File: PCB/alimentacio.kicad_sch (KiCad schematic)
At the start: 10 parts, among them J1 PowerIN, U1 LT1528CT-PBF

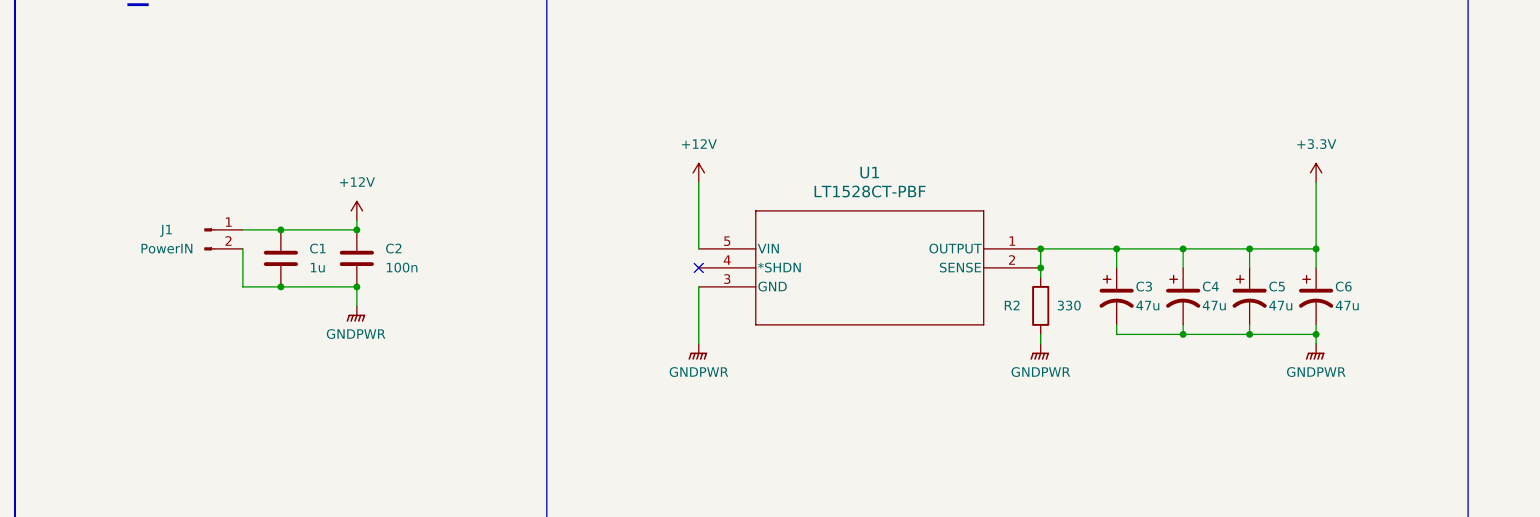
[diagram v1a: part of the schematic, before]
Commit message: correct schematic + README
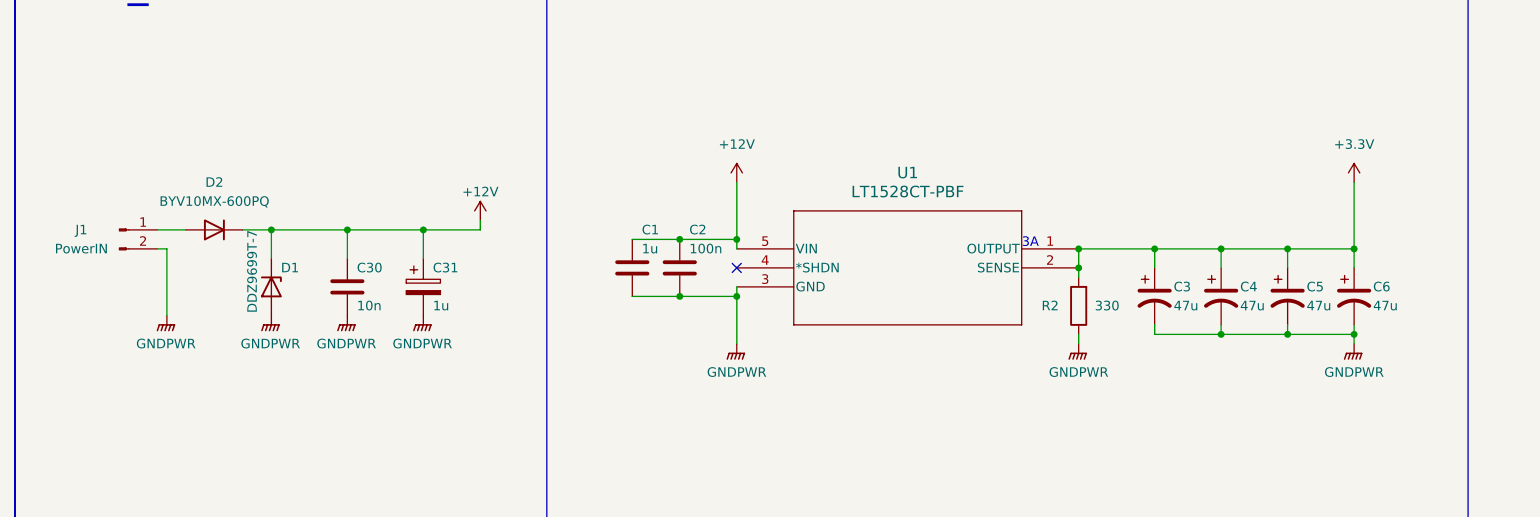
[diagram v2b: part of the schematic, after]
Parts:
- added C30: 10n, symbol Device:C
- added C31: 1u, symbol Device:C_Polarized
- added D1: DDZ9699T-7, symbol Device:D_Zener
- added D2: BYV10MX-600PQ, symbol Device:D
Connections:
- net +12V: now also C30.1, C31.1, D1.1 (K), D2.1 (K); no longer J1.1 (Pin_1)
- net GNDPWR: now also C30.2, C31.2, D1.2 (A)
- new net: D2.2 (A), J1.1 (Pin_1)
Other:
- note added: "3A"
- moved on the sheet: C3, C4, C5, C6, J1, R2, U1

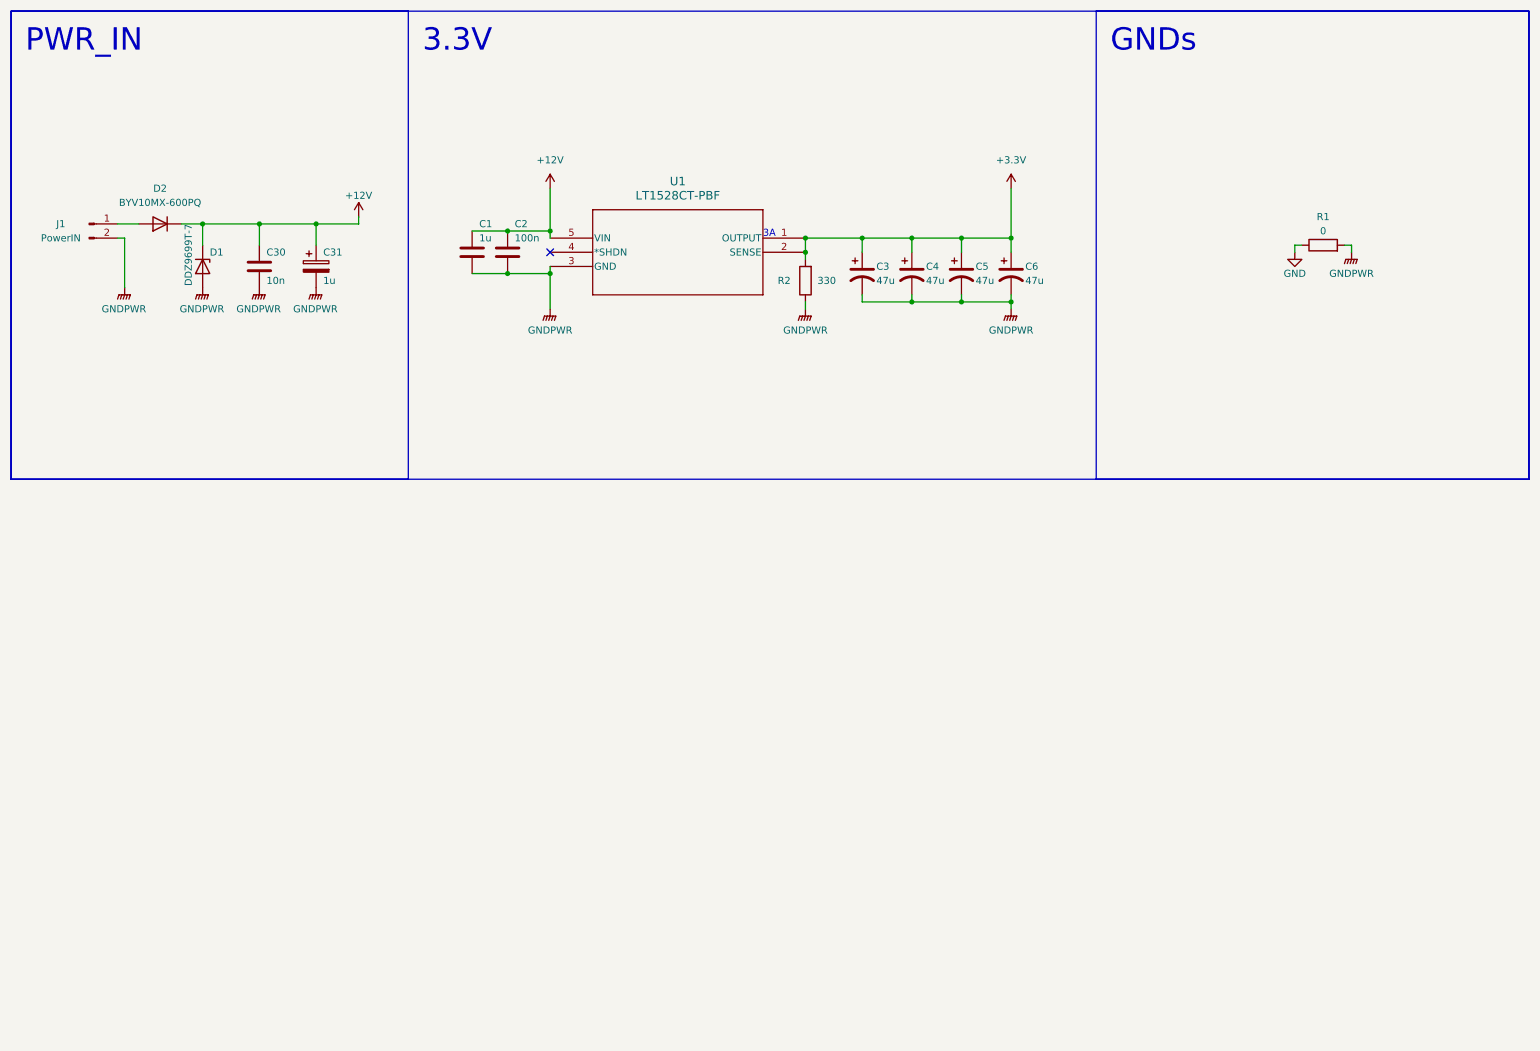
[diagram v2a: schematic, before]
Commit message: changed to DCDC 3.3V, added extra bit for window ctrl + misc corrections
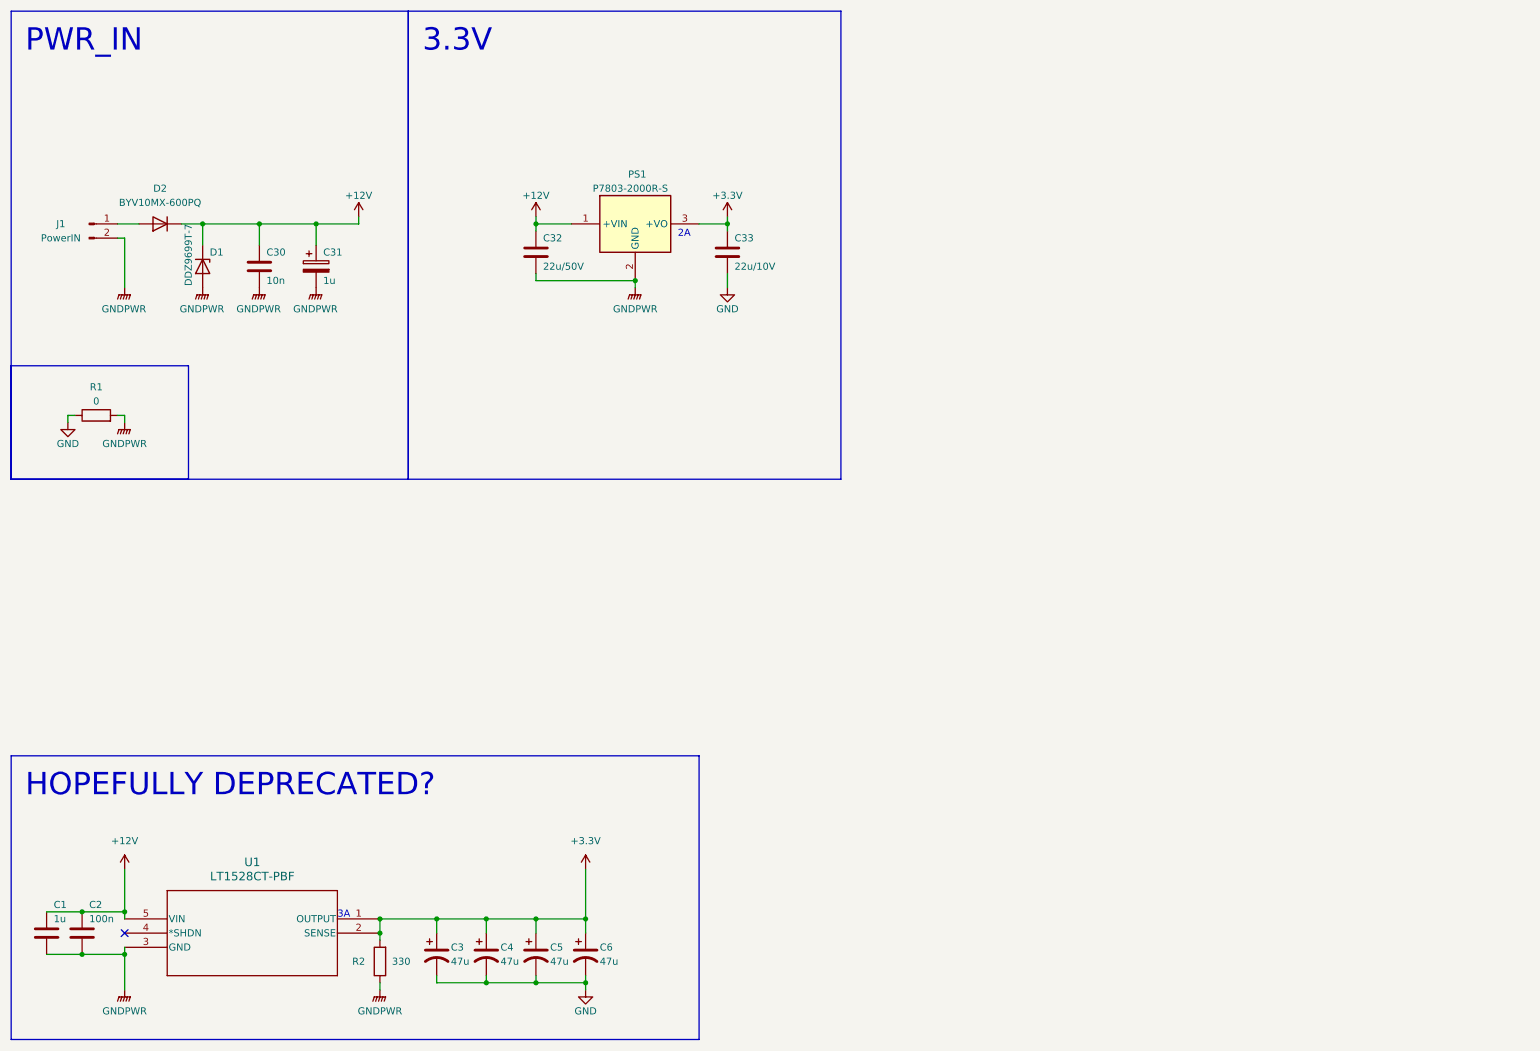
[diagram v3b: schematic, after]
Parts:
- added C32: 22u/50V, symbol Device:C
- added C33: 22u/10V, symbol Device:C
- added PS1: P7803-2000R-S, P78032000RS, symbol P7803-2000R-S:P7803-2000R-S
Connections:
- net +12V: now also C32.1, PS1.1 (+VIN)
- net +3.3V: now also C33.1, PS1.3 (+VO)
- net GND: now also C3.2, C4.2, C5.2, C6.2, C33.2
- net GNDPWR: now also C32.2, PS1.2 (GND); no longer C3.2, C4.2, C5.2, C6.2
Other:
- note added: "2A"
- note added: "HOPEFULLY DEPRECATED?"
- note removed: "GNDs"
- moved on the sheet: C1, C2, C3, C4, C5, C6, R1, R2, U1

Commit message: added all components
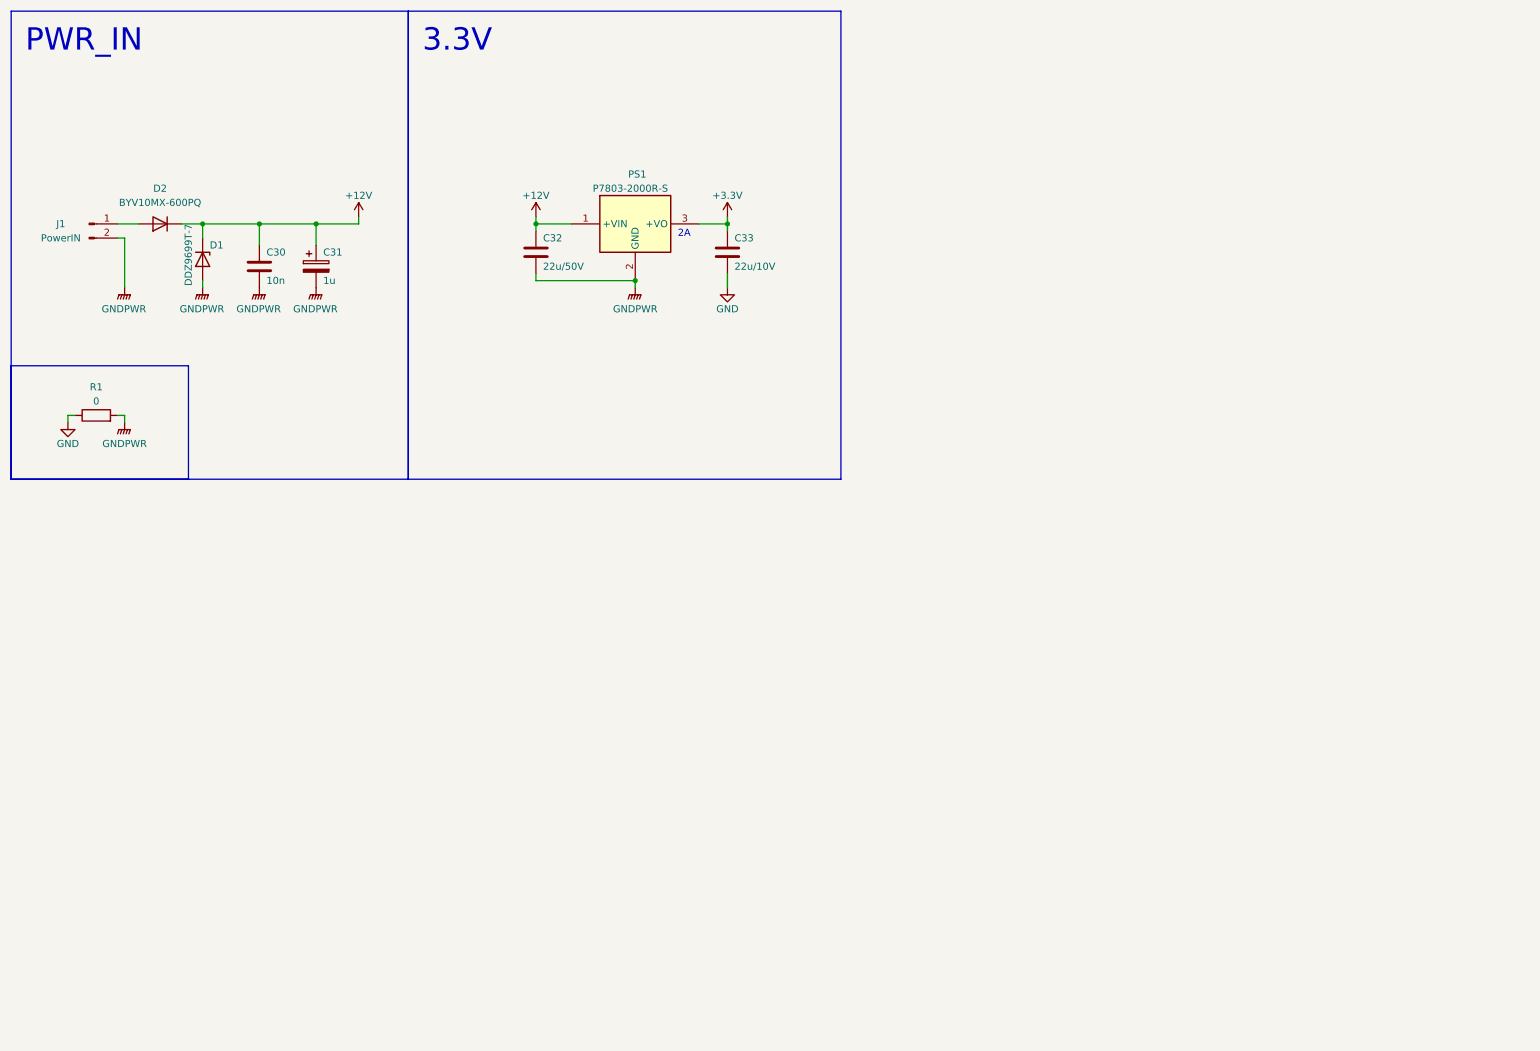
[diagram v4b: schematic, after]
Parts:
- removed C1: 1u, symbol Device:C
- removed C2: 100n, symbol Device:C
- removed C3, C4, C5, C6: 47u, symbol Device:C_Polarized_US
- removed R2: 330, symbol Device:R
- removed U1: LT1528CT-PBF, TO220-5_T_LIT, symbol LT1528CT#PBF:LT1528CT-PBF
- C30, C33: footprint (none) -> Capacitor_SMD:C_1206_3216Metric
- C31: footprint (none) -> Capacitor_Tantalum_SMD:CP_EIA-3216-18_Kemet-A
- C32: footprint (none) -> kicad_models:CAPC7563X400N
- D1: footprint (none) -> kicad_models:SODFL1608X65N
- D2: footprint (none) -> Package_TO_SOT_THT:TO-220F-2_Horizontal_TabDown
- J1: footprint (none) -> TerminalBlock_MetzConnect:TerminalBlock_MetzConnect_Type011_RT05502HBWC_1x02_P5.00mm_Horizontal
- PS1: footprint P78032000RS -> kicad_models:P78032000RS
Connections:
- no-connect marks 1 -> 0
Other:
- note removed: "3A"
- note removed: "HOPEFULLY DEPRECATED?"
- moved on the sheet: D1

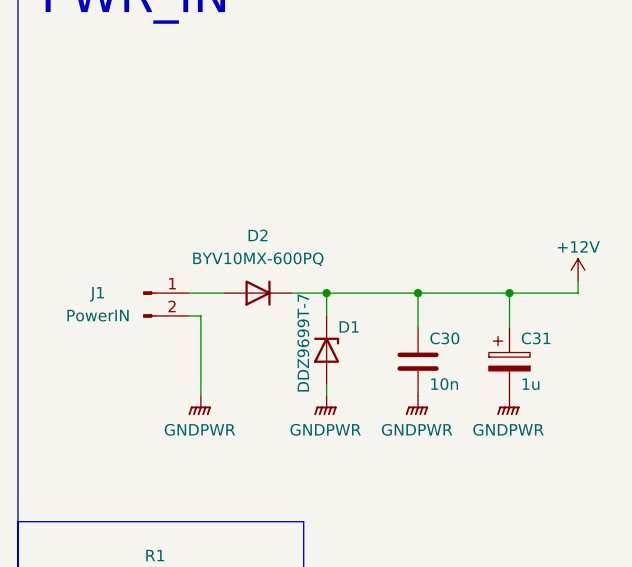
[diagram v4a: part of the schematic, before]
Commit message: power plane done
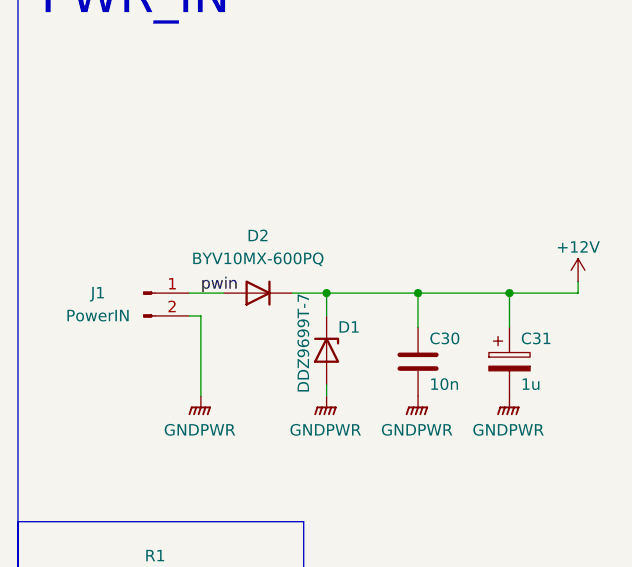
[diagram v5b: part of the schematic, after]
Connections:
- net pwin: now reaches D2.2 (A), J1.1 (Pin_1)
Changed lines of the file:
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@@
     (effects (font (size 4 4)) (justify left bottom))
+  )
+  (label "pwin" (at 33.02 50.8 0) (fields_autoplaced)
+    (effects (font (size 1.27 1.27)) (justify left bottom))
   )
   (symbol (lib_id "power:GNDPWR") (at 33.02 62.23 0) (unit 1)

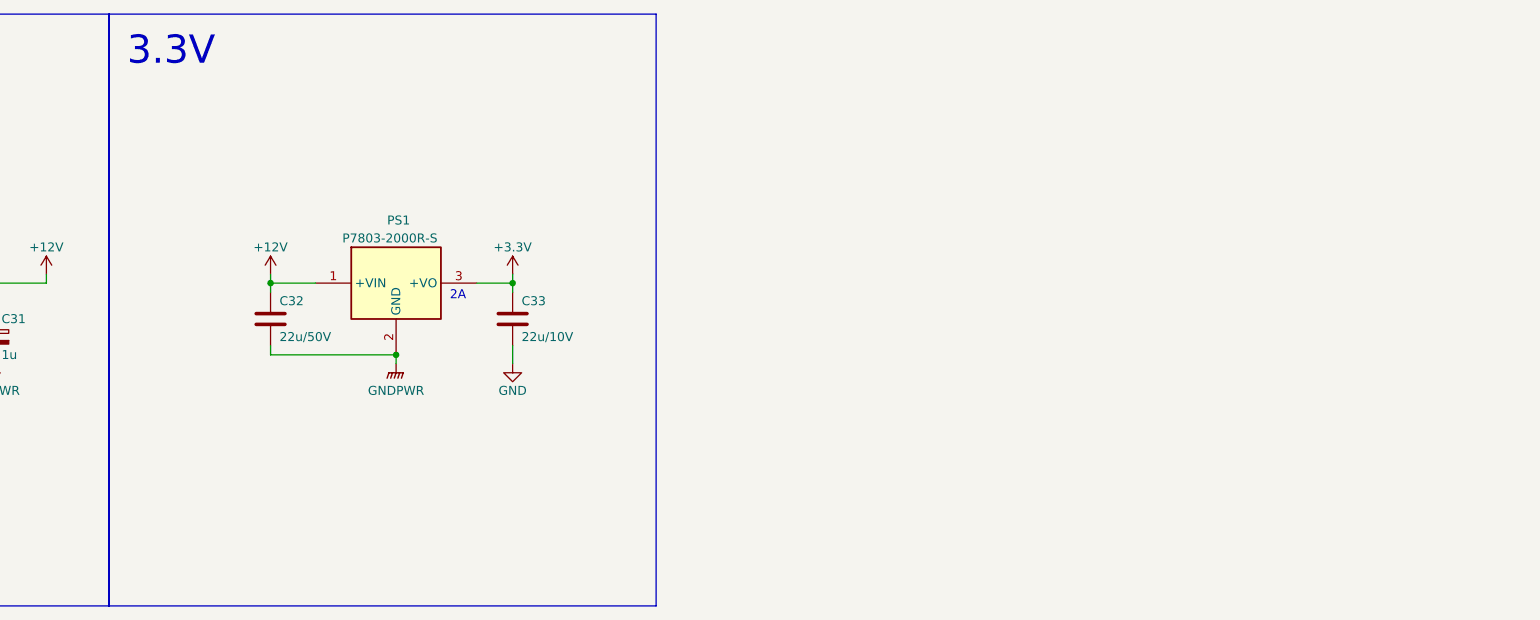
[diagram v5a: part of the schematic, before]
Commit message: added LDO from DC/DC
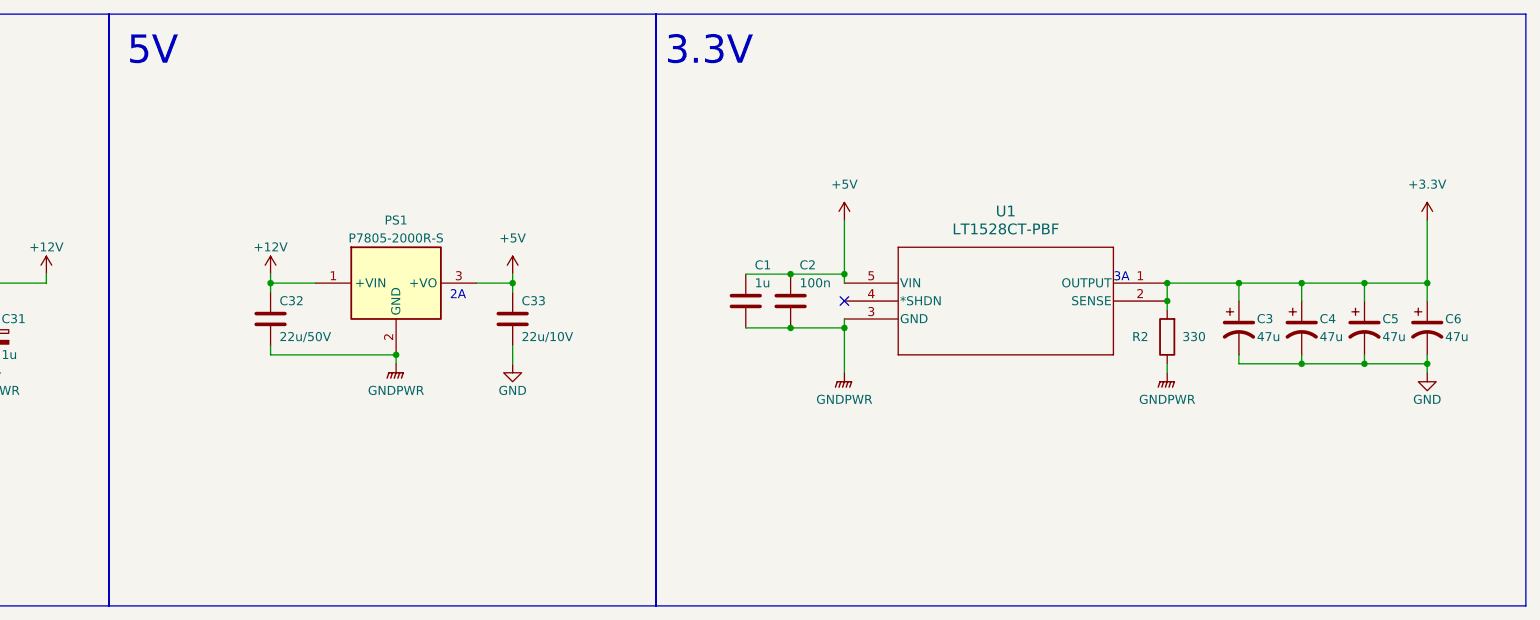
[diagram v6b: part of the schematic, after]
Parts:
- added C1: 1u, symbol Device:C
- added C2: 100n, symbol Device:C
- added C3, C4, C5, C6: 47u, symbol Device:C_Polarized_US
- added R2: 330, symbol Device:R
- added U1: LT1528CT-PBF, kicad_models:LT1528CT#PBF, symbol LT1528CT#PBF:LT1528CT-PBF
- PS1: value P7803-2000R-S -> P7805-2000R-S
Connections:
- net +3.3V: now also C3.1, C4.1, C5.1, C6.1, R2.2, U1.1 (OUTPUT), U1.2 (SENSE); no longer C33.1, PS1.3 (+VO)
- net GND: now also C3.2, C4.2, C5.2, C6.2
- net GNDPWR: now also C1.2, C2.2, R2.1, U1.3 (GND)
- new net +5V: C1.1, C2.1, C33.1, PS1.3 (+VO), U1.5 (VIN)
- no-connect marks 0 -> 1
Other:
- note added: "3A"
- note added: "5V"
